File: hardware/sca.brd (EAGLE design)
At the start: 99 x 73.3 mm, 31 parts

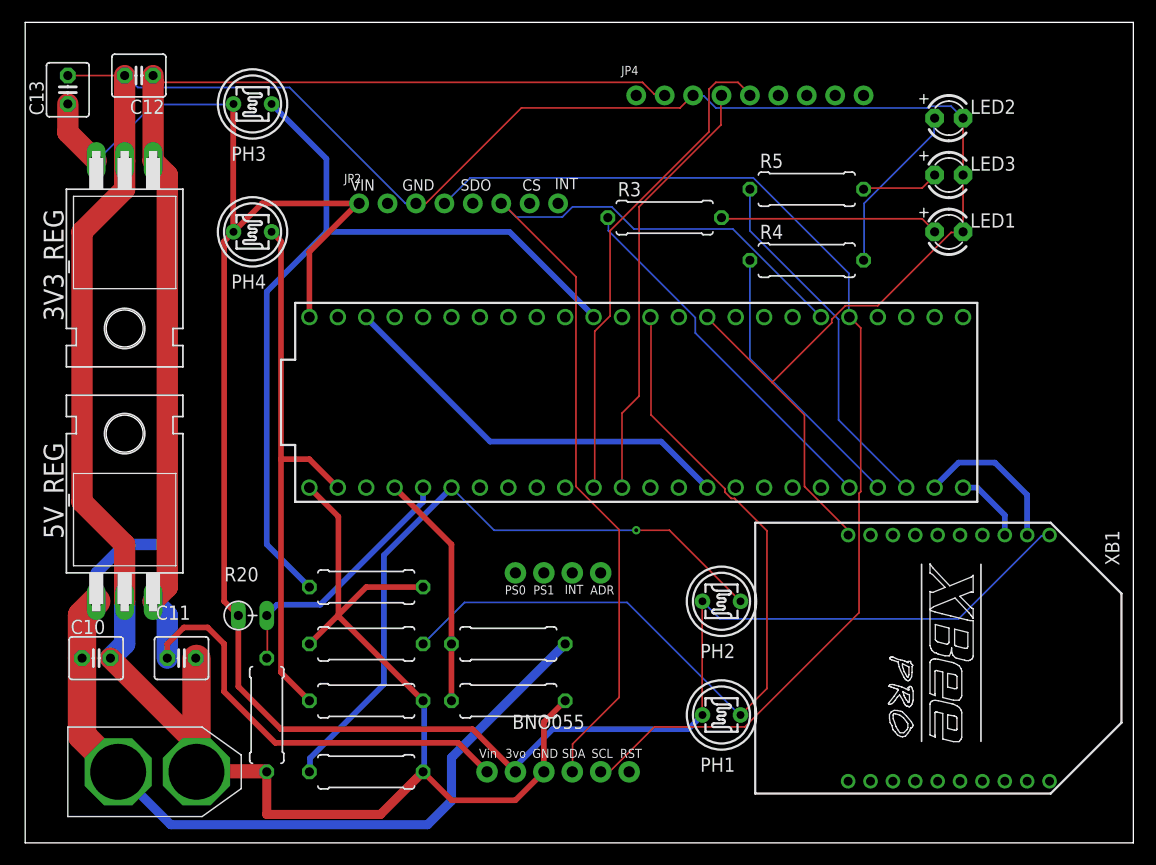
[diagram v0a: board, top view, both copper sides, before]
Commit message: preliminary routing done
adjusted some pins to optimize routing
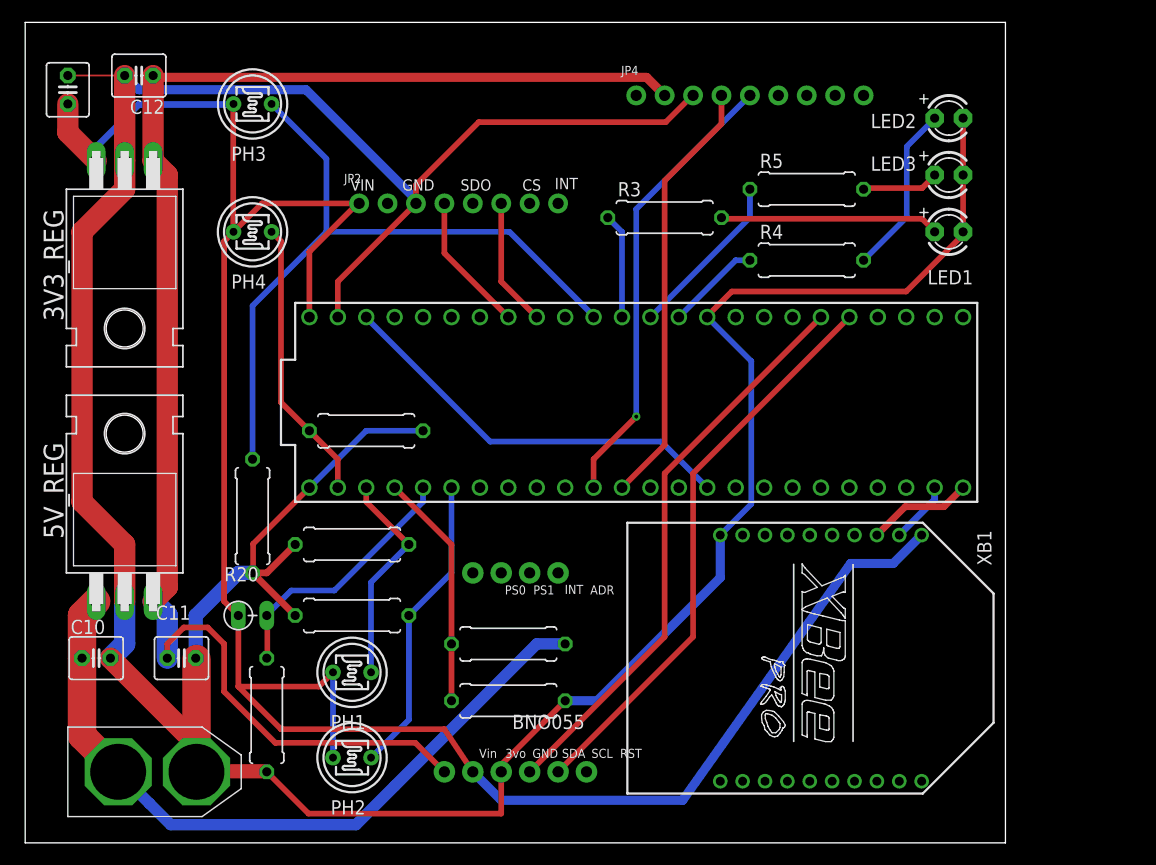
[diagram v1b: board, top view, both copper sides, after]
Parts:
- moved PH2 35.9 mm to (29.2, 7.62)
- moved PH1 33.2 mm to (29.2, 15.2)
- moved R9 24.1 mm to (30.5, 36.8)
- moved R6 14.0 mm to (29.2, 20.3), turned to 180 degrees
- moved R8 12.0 mm to (20.3, 29.2), turned to 270 degrees
- moved XB1 11.4 mm to (71.1, 16.5)
- moved R7 8.98 mm to (29.2, 26.7)
- moved JP7 3.81 mm to (43.8, 6.35)
- moved JP8 3.81 mm to (43.8, 24.1)
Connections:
- removed net AGND: U$9.AGND
- new net ALT_SCL: JP2.4, U$9.19/A5
- new net ALT_SDA: JP2.6, U$9.18/A4
- net GND: now also U$9.AGND
- net LED_1: now also U$9.15/A1; no longer U$9.28
- net LED_2: now also U$9.13; no longer U$9.29
- net LED_3: now also U$9.14/A0; no longer U$9.30
- net PR_1: now also U$9.1; no longer U$9.14/A0
- net SCL: no longer JP2.4
- net SDA: no longer JP2.6
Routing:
- net PR_1: track 75.1 -> 19.5 mm
- net SCL: track 100.4 -> 51.4 mm
- net SDA: track 90.5 -> 51.4 mm
- net PR_2: track 60.7 -> 27.1 mm, vias 1 -> 0
- net PR_4: track 49.6 -> 25.3 mm
- net LED_1: track 33.1 -> 9.42 mm
- net LED_3: track 32.5 -> 15.1 mm
- net LED_2: track 25.1 -> 8.45 mm
- net ALT_SCL: track 0.00 -> 12.5 mm
- net PR_3: track 76.1 -> 63.6 mm
- net V_BATT: track 77.9 -> 65.7 mm
- net ALT_SDA: track 0.00 -> 11.5 mm
- net XBEE_TX: track 14.0 -> 5.55 mm
- net GND: track 315.5 -> 323.3 mm
- net +5V: track 138.2 -> 134.5 mm
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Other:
- board size 99 x 73.3 mm -> 87.6 x 73.3 mm

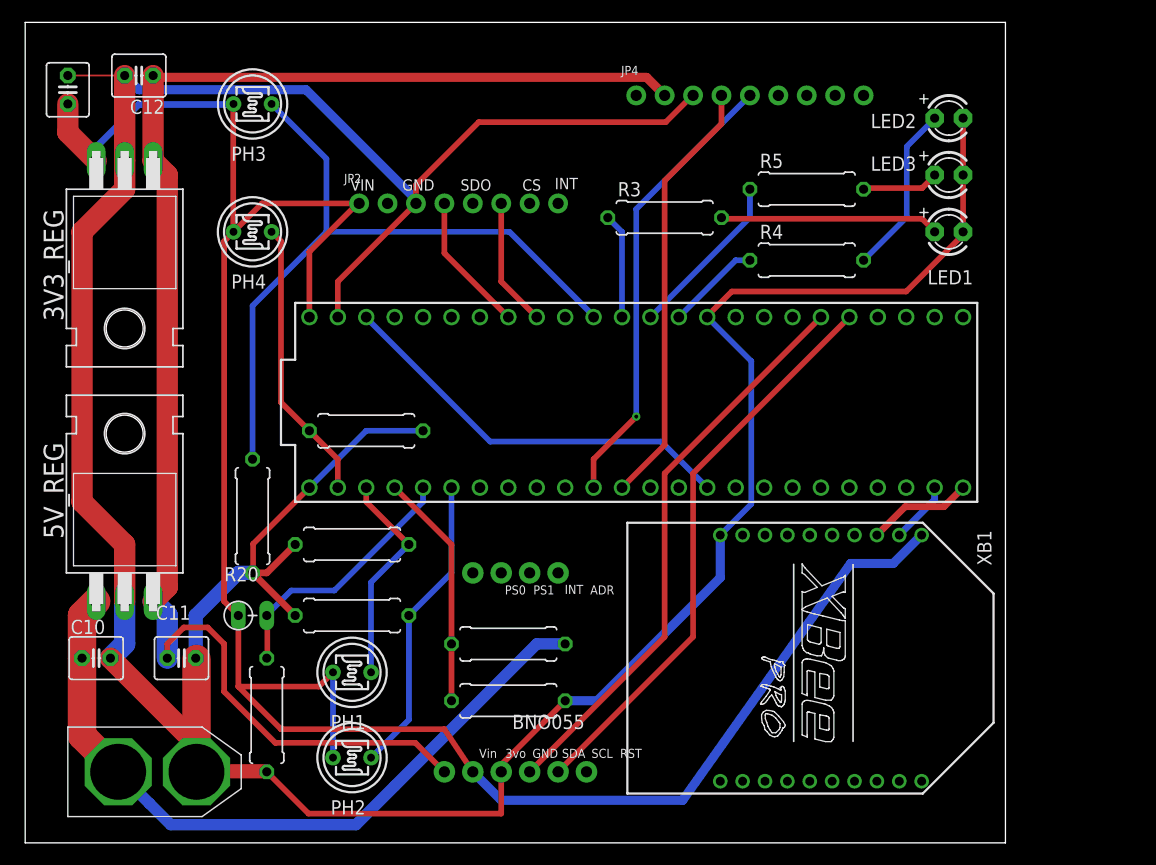
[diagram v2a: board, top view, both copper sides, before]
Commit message: removed IMU 3V3 output
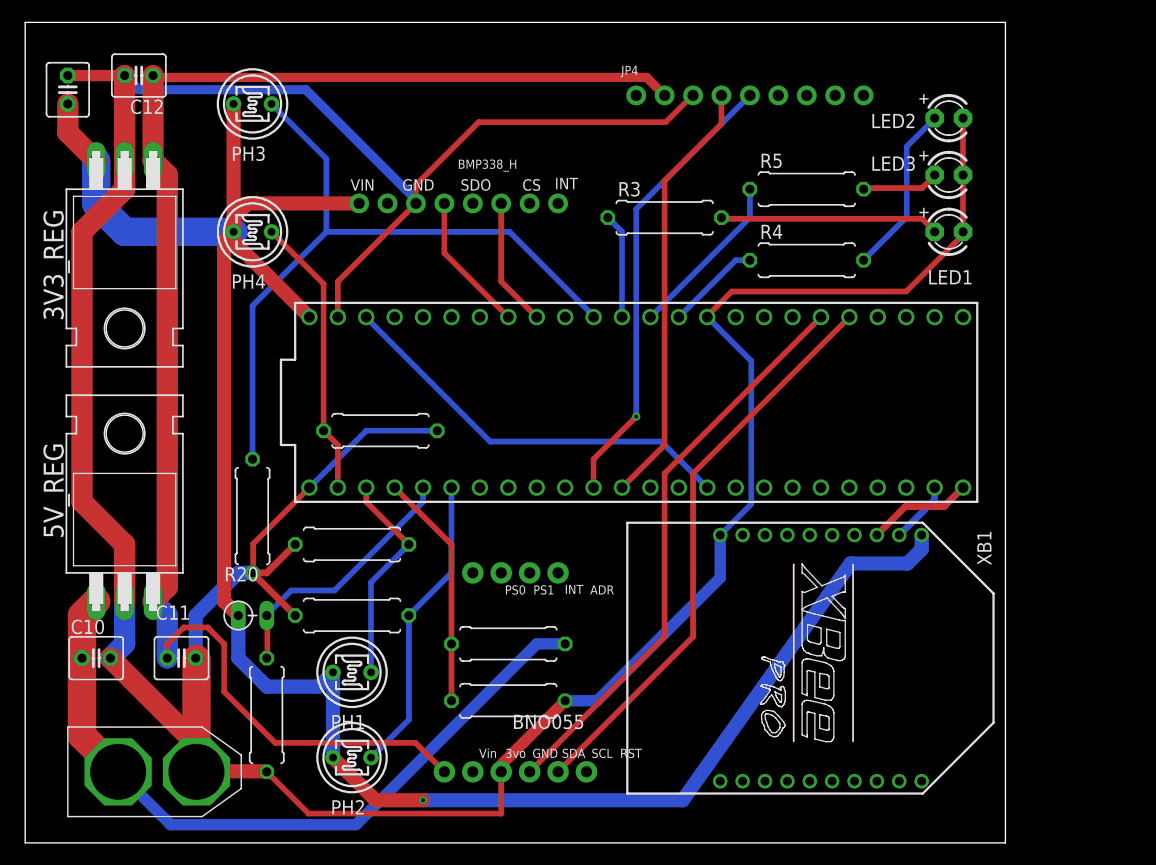
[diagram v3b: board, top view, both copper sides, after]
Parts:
- moved R9 1.27 mm to (31.8, 36.8)
- renumbered JP2 to BMP338_H, JP7 to BNO055_H1, JP8 to BNO055_H2
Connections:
- net ENABLE renamed GPS_EN
- new net 3VOUT: BNO055_H1.2
- net +3V3: no longer BNO055_H1.2
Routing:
- net +3V3: track 192.7 -> 181.7 mm, vias 0 -> 1
- net GND: track 323.3 -> 324.6 mm

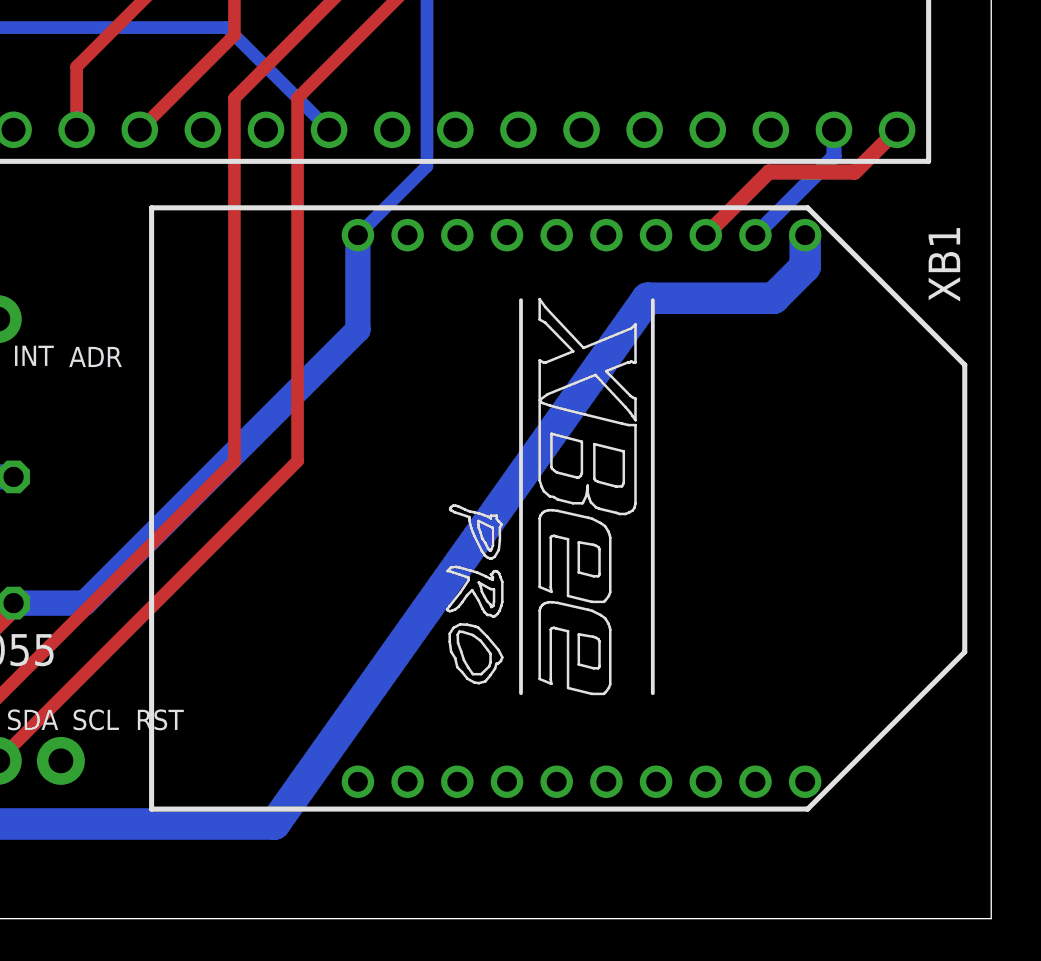
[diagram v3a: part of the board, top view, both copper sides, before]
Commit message: added Xbee EN and Vref
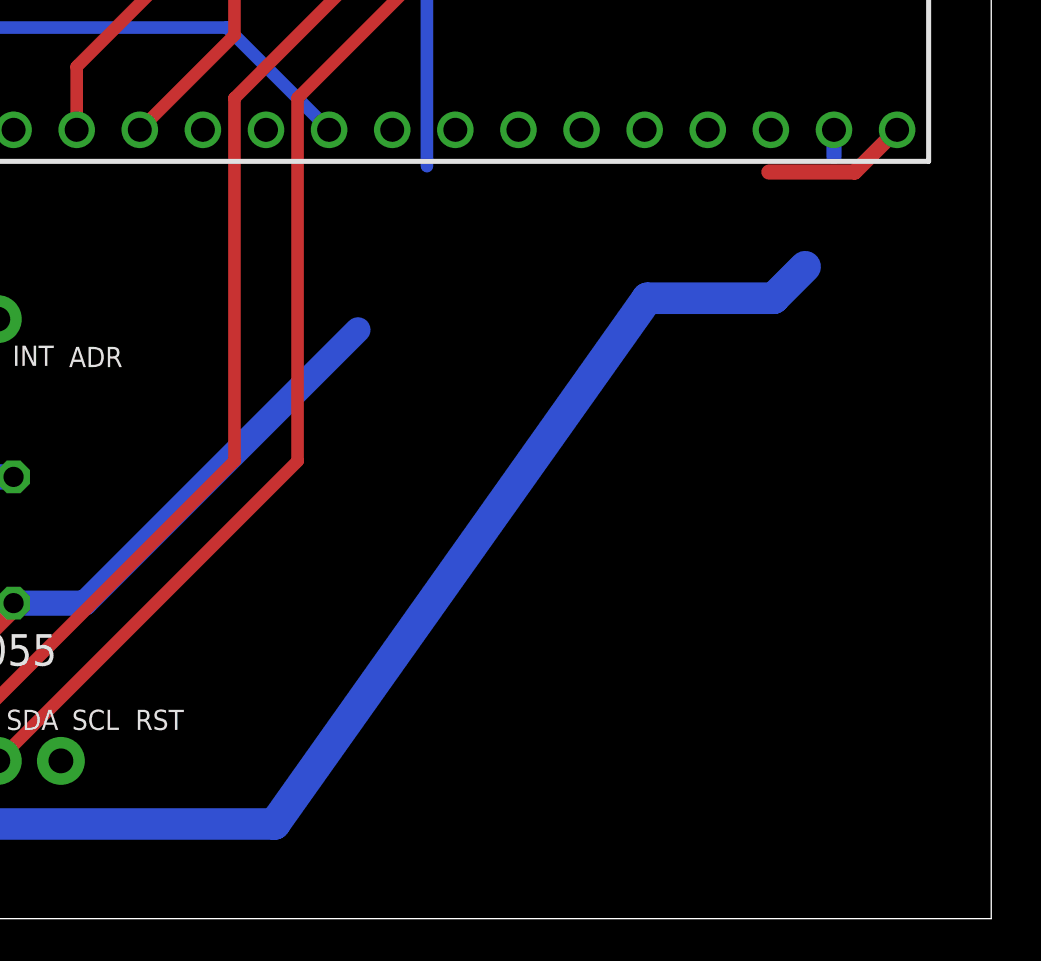
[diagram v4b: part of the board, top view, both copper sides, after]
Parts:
- removed XB1: XBEE-PRO, maxstream:XBEE-PRO
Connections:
- net +3V3: no longer XB1.1
- net GND: no longer XB1.10
- net XBEE_RX: no longer XB1.3
- net XBEE_TX: no longer XB1.2
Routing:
- net GND: track 324.6 -> 316.9 mm
- net XBEE_TX: track 5.55 -> 1.08 mm
- net XBEE_RX: track 9.46 -> 5.86 mm
- net +3V3: track 181.7 -> 180.4 mm
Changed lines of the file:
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@@
 <attribute name="NAME" x="17.78" y="23.368" size="1.27" layer="25" ratio="10"/>
-</element>
-<element name="XB1" library="maxstream" library_urn="urn:adsk.eagle:library:270" package="XBEE-PRO" package3d_urn="urn:adsk.eagle:package:18008/1" value="XBEE-PRO" x="71.12" y="16.51" smashed="yes" rot="R270">
-<attribute name="MF" value="" x="50.8" y="-8.89" size="1.778" layer="27" rot="R270" display="off"/>
-<attribute name="MPN" value="XBP24-AWI-001" x="50.8" y="-8.89" size="1.778" layer="27" rot="R270" display="off"/>
-<attribute name="NAME" x="85.09" y="27.94" size="1.27" layer="25" rot="R270"/>
-<attribute name="OC_FARNELL" value="1337916" x="50.8" y="-8.89" size="1.778" layer="27" rot="R270" display="off"/>
-<attribute name="OC_NEWARK" value="42M2667" x="50.8" y="-8.89" size="1.778" layer="27" rot="R270" display="off"/>
-<attribute name="VALUE" x="60.71" y="21.59" size="1.27" layer="27" rot="R270"/>
 </element>
 <element name="BNO055_H1" library="microbuilder" package="1X06_ROUND_76" value="" x="43.815" y="6.35" smashed="yes">
@@
 <contactref element="C12" pad="2"/>
 <contactref element="C13" pad="2"/>
-<contactref element="XB1" pad="10"/>
 <contactref element="BNO055_H1" pad="3"/>
 <contactref element="BMP338_H" pad="3"/>
@@
 <wire x1="42.545" y1="6.35" x2="42.545" y2="6.985" width="0.508" layer="1"/>
 <wire x1="42.545" y1="6.35" x2="42.545" y2="2.6162" width="0.508" layer="1"/>
-<wire x1="62.12" y1="23.7" x2="62.12" y2="27.51" width="1.016" layer="16"/>
-<wire x1="62.12" y1="27.51" x2="64.897" y2="30.287" width="0.508" layer="16"/>
 <wire x1="64.897" y1="30.287" x2="64.897" y2="43.053" width="0.508" layer="16"/>
+<wire x1="62.12" y1="23.7" x2="64.897" y2="30.287" width="0" layer="19" extent="16-16"/>
 </signal>
 <signal name="GPS_EN">
@@
 <contactref element="3V3_REG" pad="3"/>
 <contactref element="C13" pad="1"/>
-<contactref element="XB1" pad="1"/>
 <contactref element="BMP338_H" pad="1"/>
 <wire x1="6.35" y1="60.96" x2="3.81" y2="63.5" width="1.905" layer="1"/>
@@
 <wire x1="73.77" y1="24.97" x2="58.7656375" y2="3.81" width="1.27" layer="16"/>
 <wire x1="80.12" y1="26.24" x2="78.85" y2="24.97" width="1.27" layer="16"/>
-<wire x1="80.12" y1="26.24" x2="80.12" y2="27.51" width="1.27" layer="16"/>
 <wire x1="78.85" y1="24.97" x2="73.77" y2="24.97" width="1.27" layer="16"/>
 <wire x1="19.89" y1="57.15" x2="18.62" y2="55.88" width="1.27" layer="1"/>
@@
 <signal name="XBEE_TX">
 <contactref element="U$9" pad="31/A12"/>
-<contactref element="XB1" pad="2"/>
 <wire x1="81.28" y1="31.75" x2="81.28" y2="30.66996875" width="0.6096" layer="16"/>
-<wire x1="78.12" y1="27.51" x2="81.28" y2="30.66996875" width="0.6096" layer="16"/>
 </signal>
 <signal name="XBEE_RX">
 <contactref element="U$9" pad="32/A13"/>
-<contactref element="XB1" pad="3"/>
 <wire x1="82.12" y1="30.05" x2="78.66" y2="30.05" width="0.6096" layer="1"/>
-<wire x1="76.12" y1="27.51" x2="78.66" y2="30.05" width="0.6096" layer="1"/>
 <wire x1="82.12" y1="30.05" x2="83.82" y2="31.75" width="0.6096" layer="1"/>
 </signal>
